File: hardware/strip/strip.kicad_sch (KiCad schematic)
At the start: 39 parts, among them J105 CORTEX-DEBUG, J106 JAE_DX07S016JA3, SW101 SW_Push, SW102 SW_Push, U102 ATSAMD51G, U103 AP2112K-3.3, Y101 32k768

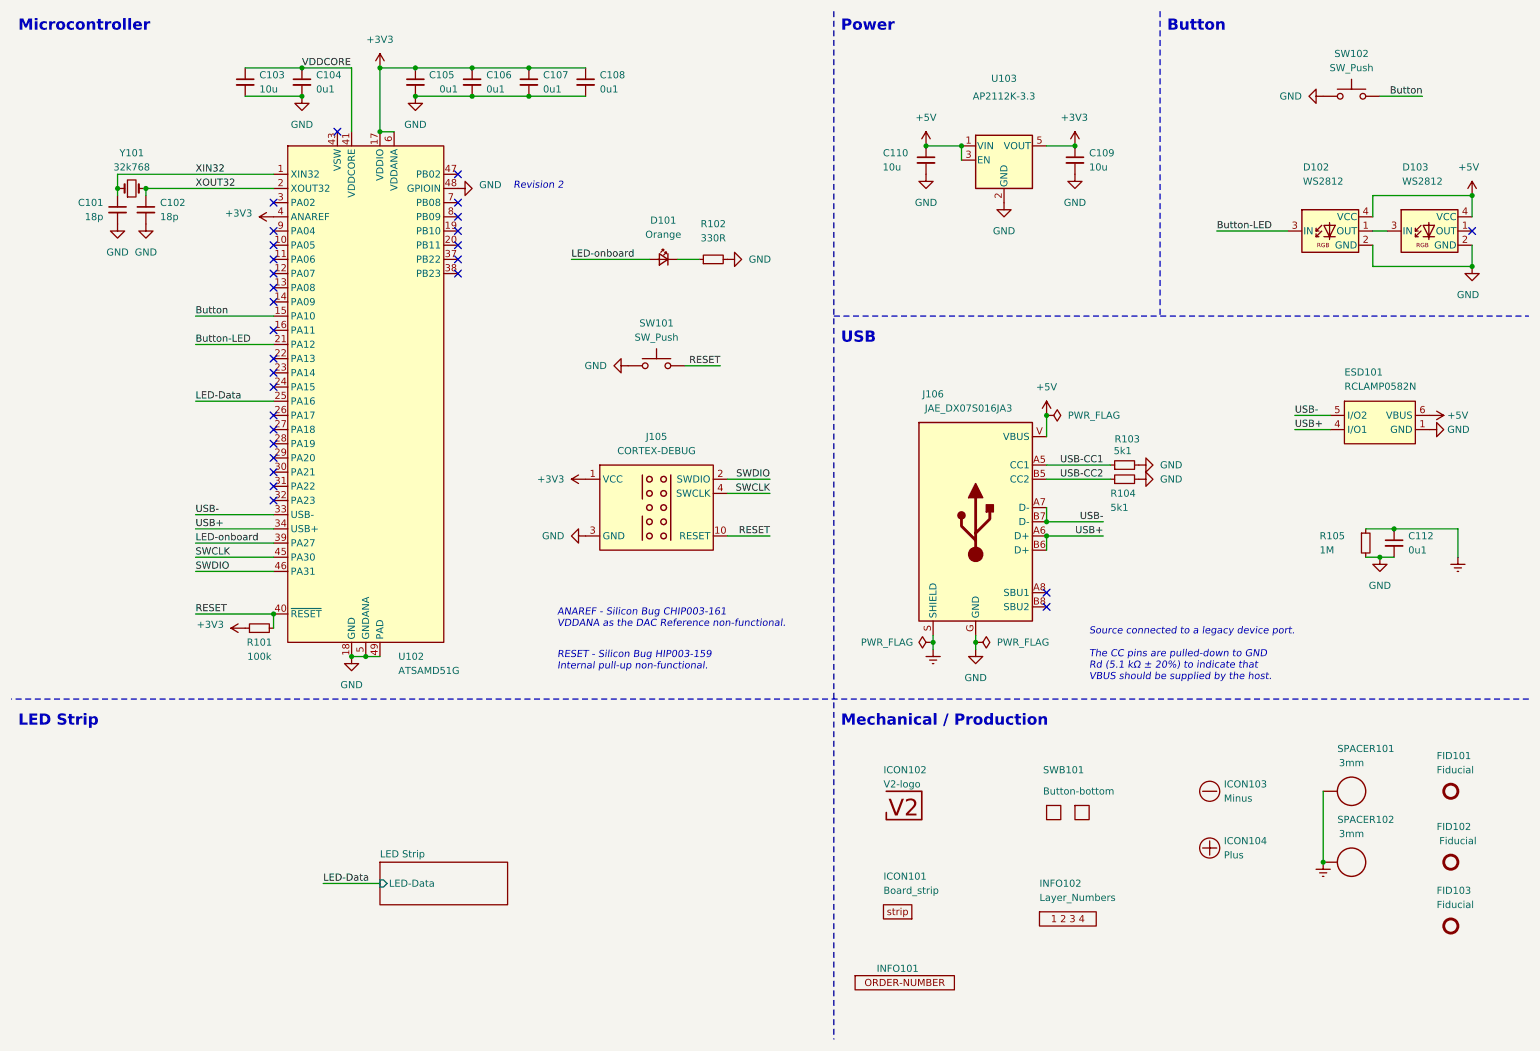
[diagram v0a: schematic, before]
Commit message: Replace Order_Number
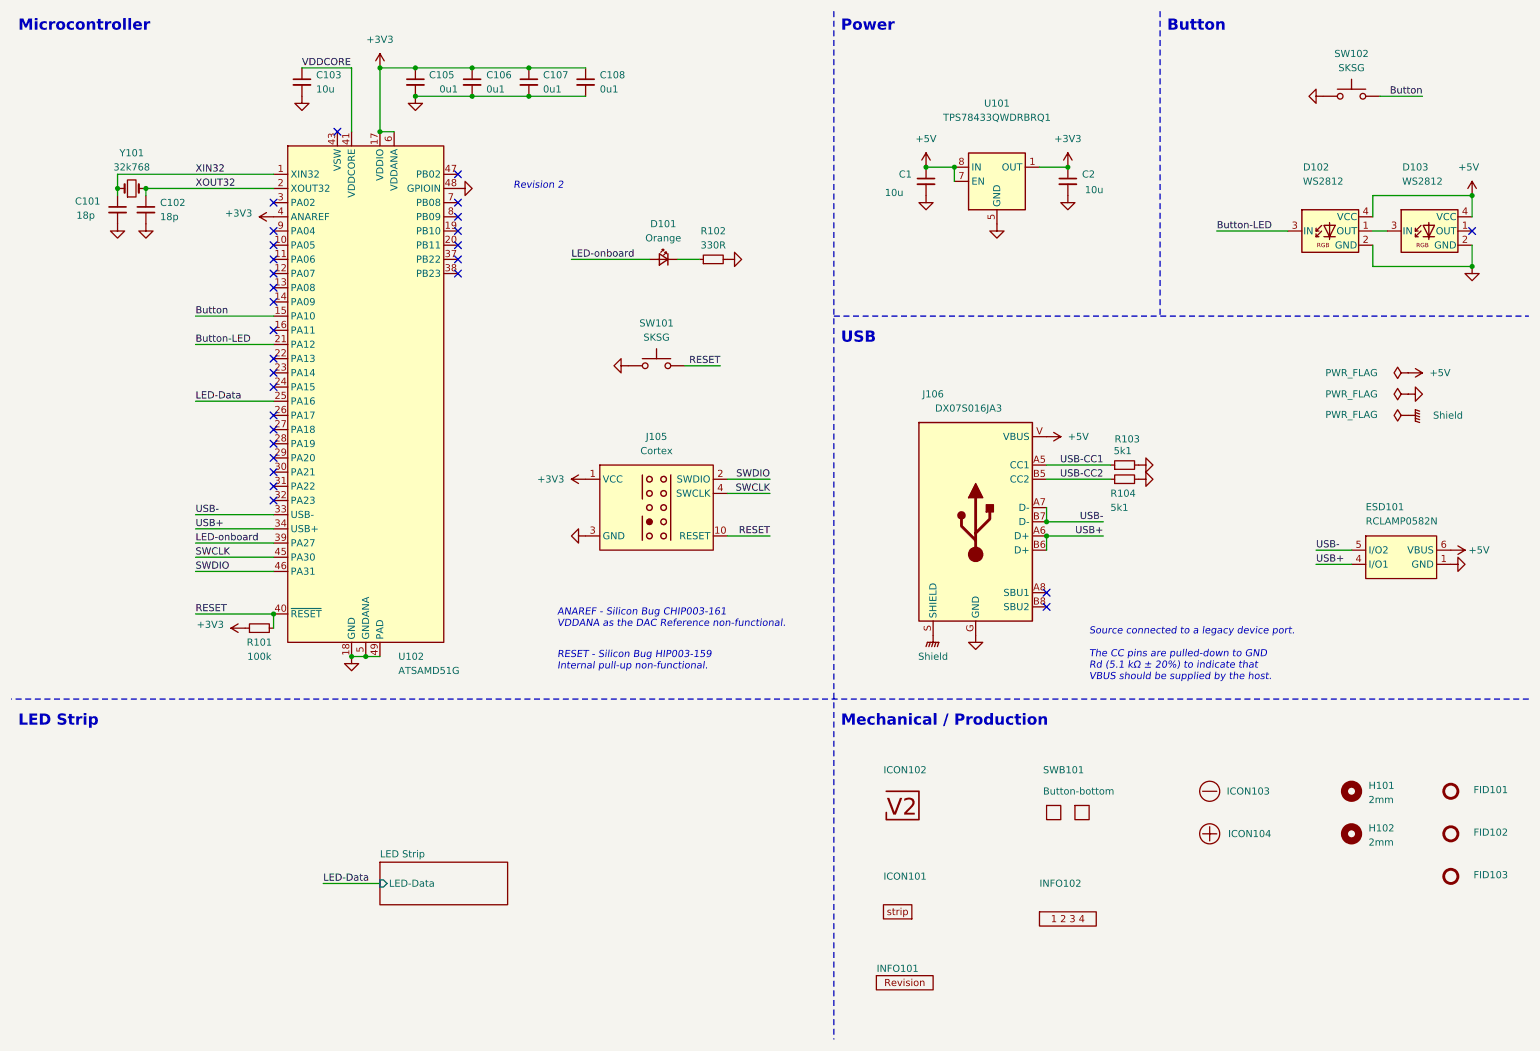
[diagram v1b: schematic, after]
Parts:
- removed C104, C112: 0u1, Capacitor_SMD:C_0603_1608Metric, symbol Device:C_Small
- removed C109, C110: 10u, Capacitor_SMD:C_0603_1608Metric, symbol Device:C_Small
- removed R105: 1M, Resistor_SMD:R_0603_1608Metric, symbol Device:R_Small
- removed SPACER101, SPACER102: 3mm, V2_Spacer_Wurth:9774030243, symbol V2_Spacer_Wurth:9774030243
- removed U103: AP2112K-3.3, Package_TO_SOT_SMD:SOT-23-5, symbol Regulator_Linear:AP2112K-3.3
- added C1, C2: 10u, V2_Capacitor_SMD:C_0805, symbol V2_Device:C_0805_10u
- added H101, H102: 2mm, V2_Mechanical:MountingHole_2mm, symbol V2_Mechanical:MountingHole_2mm
- added U101: TPS78433QWDRBRQ1, V2_Package_SON:VSON-8-1_3x3mm_P0.65_EP1.65x2.4mm, symbol V2_Regulator_Linear:TPS78433QWDRBRQ1
- C101, C102: footprint Capacitor_SMD:C_0603_1608Metric -> V2_Capacitor_SMD:C_0603; symbol Device:C_Small -> V2_Device:C_0603_18p; Manufacturer (none) -> YAGEO; Mouser (none) -> 603-CC603JRNPO9BN180; Product (none) -> CC0603JRNPO9BN180
- C103: footprint Capacitor_SMD:C_0603_1608Metric -> V2_Capacitor_SMD:C_0603; symbol Device:C_Small -> V2_Device:C_0603_10u; Manufacturer (none) -> TDK; Mouser (none) -> 810-C1608X6S1A106M; Product (none) -> C1608X6S1A106M080AC; Rating (none) -> 10V
- C105, C106, C107, C108: footprint Capacitor_SMD:C_0603_1608Metric -> V2_Capacitor_SMD:C_0603; symbol Device:C_Small -> V2_Device:C_0603_0u1; Manufacturer (none) -> TDK; Mouser (none) -> 810-CGA3E2X7R1H104MA; Product (none) -> CGA3E2X7R1H104M080AA; Rating (none) -> 50V
- D101: footprint LED_SMD:LED_0603_1608Metric -> V2_LED:LED_0603; symbol Device:LED_Small -> V2_Device:LED_0603_Orange; Manufacturer (none) -> ROHM Semiconductor; Mouser (none) -> 755-SML-D12D1WT86; Product (none) -> SML-D12D1WT86
- D102, D103: LCSC (none) -> C965555; Manufacturer (none) -> Worldsemi; Product (none) -> WS2812B-2020
- ESD101: Manufacturer (none) -> Semtech; Mouser (none) -> 947-RCLAMP0582N.TCT; Product (none) -> RCLAMP0582N.TCT
- FID101, FID102, FID103: value Fiducial -> Fiducial_Paste
- INFO101: value ORDER-NUMBER -> (none); footprint V2_Production:Order_Number -> V2_Production:Revision; symbol V2_Production:Order_Number -> V2_Production:Revision
- J105: value CORTEX-DEBUG -> Cortex; footprint V2_Cortex_Debug:Cortex_Debug_Pad -> V2_Connector_Debug:Cortex; symbol V2_Cortex_Debug:Cortex_Debug -> V2_Connector_Debug:Cortex
- J106: value JAE_DX07S016JA3 -> DX07S016JA3; Manufacturer (none) -> JAE Electronics; Mouser (none) -> 656-DX07S016JA3R1500; Product (none) -> DX07S016JA3R1500
- R101: footprint Resistor_SMD:R_0603_1608Metric -> V2_Resistor_SMD:R_0603; symbol Device:R_Small -> V2_Device:R_0603_100k; Manufacturer (none) -> Vishay; Mouser (none) -> 71-CRCW0603100KFKEAC; Product (none) -> CRCW0603100KFKEAC; Rating (none) -> 100mW
- R102: footprint Resistor_SMD:R_0603_1608Metric -> V2_Resistor_SMD:R_0603; symbol Device:R_Small -> V2_Device:R_0603_330R; Manufacturer (none) -> Vishay; Mouser (none) -> 71-CRCW0603330RFKEAC; Product (none) -> CRCW0603330RFKEAC; Rating (none) -> 100mW
- R103, R104: footprint Resistor_SMD:R_0603_1608Metric -> V2_Resistor_SMD:R_0603; symbol Device:R_Small -> V2_Device:R_0603_5k1; Manufacturer (none) -> Vishay; Mouser (none) -> 71-CRCW06035K10FKEAC; Product (none) -> CRCW06035K10FKEAC; Rating (none) -> 100mW
- SW101, SW102: value SW_Push -> SKSG; symbol Switch:SW_Push -> V2_Switch:SKSG; Manufacturer (none) -> Alps Alpine; Mouser (none) -> 688-SKSGACE010; Product (none) -> SKSGACE010
- U102: Manufacturer (none) -> Microchip Technology; Mouser (none) -> 556-ATSAMD51G19AMU; Product (none) -> ATSAMD51G19A-MU
- Y101: symbol Device:Crystal_Small -> V2_Device:Crystal_3.2x1.5_32k768; Manufacturer (none) -> ABRACON; Mouser (none) -> 815-ABS0716632.768KT; Product (none) -> ABS07-166-32.768KHZ-T
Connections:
- net +3V3: now also C2.1, U101.1 (OUT)
- net +5V: now also C1.1, U101.7 (EN), U101.8 (IN)
- net GND: now also C1.2, C2.2, U101.5 (GND), U101.9 (GND)
- net Earth renamed Shield
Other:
- moved on the sheet: C103, ESD101, FID102, FID103, ICON104

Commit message: Update Library
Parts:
- C1, C2: symbol V2_Device:C_0805_10u -> V2_Capacitor:0805_10u
- C101, C102: symbol V2_Device:C_0603_18p -> V2_Capacitor:0603_18p
- C103: symbol V2_Device:C_0603_10u -> V2_Capacitor:0603_10u
- C105, C106, C107, C108: symbol V2_Device:C_0603_0u1 -> V2_Capacitor:0603_0u1
- D101: symbol V2_Device:LED_0603_Orange -> V2_LED:0603_Orange
- INFO101: value (none) -> ~
- R101: symbol V2_Device:R_0603_100k -> V2_Resistor:0603_100k
- R102: symbol V2_Device:R_0603_330R -> V2_Resistor:0603_330R
- R103, R104: symbol V2_Device:R_0603_5k1 -> V2_Resistor:0603_5k1
- Y101: symbol V2_Device:Crystal_3.2x1.5_32k768 -> V2_Crystal:3.2x1.5_32k768

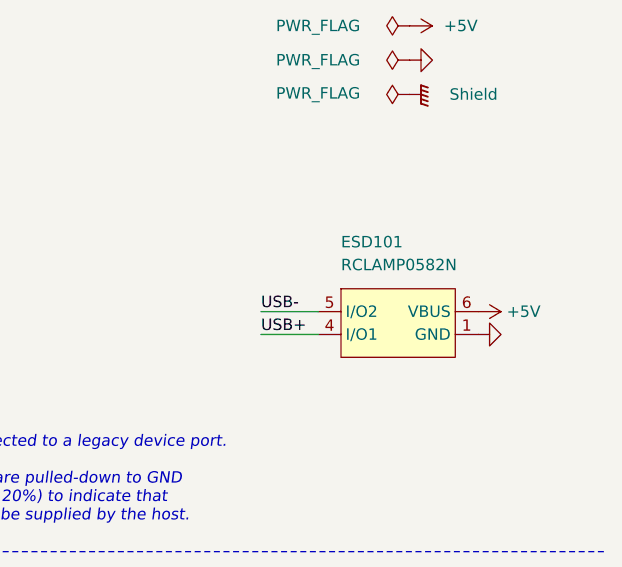
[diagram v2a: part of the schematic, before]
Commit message: Update ESD suppressor
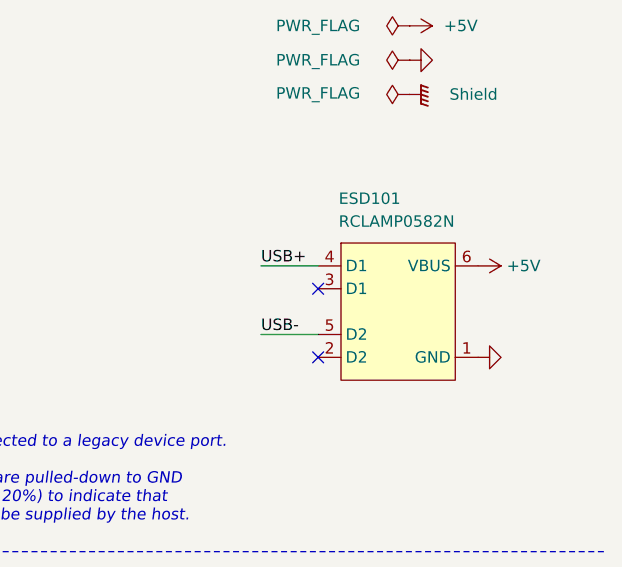
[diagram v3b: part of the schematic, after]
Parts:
- C101, C102: Manufacturer YAGEO -> TDK; Mouser 603-CC603JRNPO9BN180 -> 810-CGA3E2C0G1H180J; Product CC0603JRNPO9BN180 -> CGA3E2C0G1H180J080AA
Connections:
- no-connect marks 29 -> 31
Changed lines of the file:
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@@
 	(title_block
 		(title "V2 strip")
-		(date "2026-02-11")
+		(date "2026-03-14")
 		(rev "2026-02-11")
 		(company "Versio Duo")
@@
 	)
 	(no_connect
+		(at 252.73 106.68)
+	)
+	(no_connect
 		(at 274.32 52.07)
 	)
@@
 		(at 59.69 100.33)
 	)
+	(no_connect
+		(at 252.73 114.3)
+	)
 	(wire
 		(pts
@@
 	(wire
 		(pts
-			(xy 246.38 109.22) (xy 252.73 109.22)
+			(xy 246.38 111.76) (xy 252.73 111.76)
 		)
 		(stroke
@@
 	(wire
 		(pts
-			(xy 73.66 128.27) (xy 76.2 128.27)
+			(xy 246.38 104.14) (xy 252.73 104.14)
 		)
 		(stroke
@@
 	(wire
 		(pts
-			(xy 45.72 110.49) (xy 59.69 110.49)
+			(xy 73.66 128.27) (xy 76.2 128.27)
 		)
 		(stroke
@@
 	(wire
 		(pts
-			(xy 198.12 104.14) (xy 208.28 104.14)
+			(xy 45.72 110.49) (xy 59.69 110.49)
 		)
 		(stroke
@@
 	(wire
 		(pts
-			(xy 78.74 34.29) (xy 81.28 34.29)
+			(xy 198.12 104.14) (xy 208.28 104.14)
 		)
 		(stroke
@@
 	(wire
 		(pts
-			(xy 76.2 128.27) (xy 78.74 128.27)
+			(xy 78.74 34.29) (xy 81.28 34.29)
 		)
 		(stroke
@@
 	(wire
 		(pts
-			(xy 198.12 106.68) (xy 198.12 109.22)
+			(xy 76.2 128.27) (xy 78.74 128.27)
 		)
 		(stroke
@@
 	(wire
 		(pts
-			(xy 45.72 102.87) (xy 59.69 102.87)
+			(xy 198.12 106.68) (xy 198.12 109.22)
 		)
 		(stroke
@@
 	(wire
 		(pts
-			(xy 246.38 111.76) (xy 252.73 111.76)
+			(xy 45.72 102.87) (xy 59.69 102.87)
 		)
 		(stroke
@@
 		)
 	)
+	(label "USB+"
+		(at 246.38 104.14 0)
+		(effects
+			(font
+				(size 1.27 1.27)
+			)
+			(justify left bottom)
+		)
+	)
 	(label "USB-CC2"
 		(at 208.28 96.52 180)
@@
 		)
 	)
-	(label "USB+"
-		(at 246.38 111.76 0)
-		(effects
-			(font
-				(size 1.27 1.27)
-			)
-			(justify left bottom)
-		)
-	)
 	(label "SWDIO"
 		(at 148.59 96.52 180)
@@
 	)
 	(label "USB-"
-		(at 246.38 109.22 0)
+		(at 246.38 111.76 0)
 		(effects
 			(font
@@
 			)
 		)
-		(property "Description" "Resistor, small symbol"
+		(property "Description" ""
 			(at 224.79 93.98 0)
 			(effects
@@
 			)
 		)
-		(property "Description" "Unpolarized capacitor, small symbol"
+		(property "Description" ""
 			(at 115.57 38.1 0)
 			(effects
@@
 		(dnp no)
 		(property "Reference" "ESD101"
-			(at 255.27 102.235 0)
+			(at 255.016 97.409 0)
 			(effects
 				(font
@@
 		)
 		(property "Value" "RCLAMP0582N"
-			(at 255.27 104.775 0)
+			(at 255.016 99.949 0)
 			(effects
 				(font
@@
 		(at 227.33 152.4 0)
 		(unit 1)
-		(exclude_from_sim no)
+		(exclude_from_sim yes)
 		(in_bom no)
 		(on_board yes)
@@
 			)
 		)
-		(property "Sim.Enable" "0"
-			(at 227.33 152.4 0)
-			(effects
-				(font
-					(size 1.27 1.27)
-				)
-				(hide yes)
-			)
-		)
 		(instances
 			(project "strip"
@@
 			)
 		)
-		(property "Description" "Push button switch, generic, two pins"
+		(property "Description" "Push button"
 			(at 252.73 27.94 0)
 			(effects
@@
 	(symbol
 		(lib_id "V2_power:+5V")
-		(at 270.51 109.22 270)
+		(at 270.51 104.14 270)
 		(unit 1)
 		(exclude_from_sim no)
@@
 		(fields_autoplaced yes)
 		(property "Reference" "#PWR130"
-			(at 266.7 109.22 0)
+			(at 266.7 104.14 0)
 			(effects
 				(font
@@
 		)
 		(property "Value" "+5V"
-			(at 273.685 109.2199 90)
+			(at 273.685 104.1399 90)
 			(effects
 				(font
@@
 		)
 		(property "Footprint" ""
-			(at 270.51 109.22 0)
+			(at 270.51 104.14 0)
 			(effects
 				(font
@@
 		)
 		(property "Datasheet" ""
-			(at 270.51 109.22 0)
+			(at 270.51 104.14 0)
 			(effects
 				(font
@@
 		)
 		(property "Description" ""
-			(at 270.51 109.22 0)
+			(at 270.51 104.14 0)
 			(effects
 				(font
@@
 			)
 		)
-		(property "Description" "Light emitting diode, small symbol"
+		(property "Description" ""
 			(at 129.54 62.23 0)
 			(effects
@@
 		(at 201.93 156.21 0)
 		(unit 1)
-		(exclude_from_sim no)
+		(exclude_from_sim yes)
 		(in_bom no)
 		(on_board yes)
@@
 			)
 		)
-		(property "Sim.Enable" "0"
-			(at 201.93 156.21 0)
-			(effects
-				(font
-					(size 1.27 1.27)
-				)
-				(hide yes)
-			)
-		)
 		(instances
 			(project "strip"
@@
 			)
 		)
-		(property "Description" "Unpolarized capacitor, small symbol"
+		(property "Description" ""
 			(at 176.53 56.642 0)
 			(effects
@@
 			)
 		)
-		(property "Description" "Two pin crystal, small symbol"
+		(property "Description" ""
 			(at 34.29 44.45 0)
 			(effects
@@
 			)
 		)
-		(property "Description" "Unpolarized capacitor, small symbol"
+		(property "Description" ""
 			(at 36.83 62.738 0)
 			(effects
@@
 			)
 		)
-		(property "Mouser" "603-CC603JRNPO9BN180"
+		(property "Mouser" "810-CGA3E2C0G1H180J"
 			(at 36.83 71.628 0)
 			(effects
@@
 			)
 		)
-		(property "Product" "CC0603JRNPO9BN180"
+		(property "Product" "CGA3E2C0G1H180J080AA"
 			(at 36.83 68.834 0)
 			(effects
@@
 			)
 		)
-		(property "Manufacturer" "YAGEO"
+		(property "Manufacturer" "TDK"
 			(at 36.83 66.04 0)
 			(effects
@@
 			)
 		)
-		(property "Description" "Unpolarized capacitor, small symbol"
+		(property "Description" ""
 			(at 64.77 40.64 0)
 			(effects
@@
 			)
 		)
-		(property "Description" "Unpolarized capacitor, small symbol"
+		(property "Description" ""
 			(at 31.75 62.738 0)
 			(effects
@@
 			)
 		)
-		(property "Mouser" "603-CC603JRNPO9BN180"
+		(property "Mouser" "810-CGA3E2C0G1H180J"
 			(at 31.75 71.628 0)
 			(effects
@@
 			)
 		)
-		(property "Product" "CC0603JRNPO9BN180"
+		(property "Product" "CGA3E2C0G1H180J080AA"
 			(at 31.75 68.834 0)
 			(effects
@@
 			)
 		)
-		(property "Manufacturer" "YAGEO"
+		(property "Manufacturer" "TDK"
 			(at 31.75 66.04 0)
 			(effects
@@
 			)
 		)
-		(property "Description" "Resistor, small symbol"
+		(property "Description" ""
 			(at 151.13 57.15 0)
 			(effects
@@
 	(symbol
 		(lib_id "V2_power:GND")
-		(at 270.51 111.76 90)
+		(at 270.51 114.3 90)
 		(unit 1)
 		(exclude_from_sim no)
@@
 		(fields_autoplaced yes)
 		(property "Reference" "#PWR131"
-			(at 276.86 111.76 0)
+			(at 276.86 114.3 0)
 			(effects
 				(font
@@
 		)
 		(property "Value" "GND"
-			(at 273.685 111.7599 90)
+			(at 273.685 114.2999 90)
 			(effects
 				(font
@@
 		)
 		(property "Footprint" ""
-			(at 270.51 111.76 0)
+			(at 270.51 114.3 0)
 			(effects
 				(font
@@
 		)
 		(property "Datasheet" ""
-			(at 270.51 111.76 0)
+			(at 270.51 114.3 0)
 			(effects
 				(font
@@
 		)
 		(property "Description" ""
-			(at 270.51 111.76 0)
+			(at 270.51 114.3 0)
 			(effects
 				(font
@@
 			)
 		)
-		(property "Description" "Unpolarized capacitor, small symbol"
+		(property "Description" ""
 			(at 105.41 38.1 0)
 			(effects
@@
 			)
 		)
-		(property "Description" "Unpolarized capacitor, small symbol"
+		(property "Description" ""
 			(at 201.93 56.642 0)
 			(effects
@@
 			)
 		)
-		(property "Description" "Unpolarized capacitor, small symbol"
+		(property "Description" ""
 			(at 85.09 38.1 0)
 			(effects
@@
 			)
 		)
-		(property "Description" "Resistor, small symbol"
+		(property "Description" ""
 			(at 224.79 96.52 0)
 			(effects
@@
 			)
 		)
-		(property "Description" "Push button switch, generic, two pins"
+		(property "Description" "Push button"
 			(at 128.27 76.2 0)
 			(effects
@@
 		(at 171.45 173.99 0)
 		(unit 1)
-		(exclude_from_sim no)
+		(exclude_from_sim yes)
 		(in_bom no)
 		(on_board yes)
@@
 			)
 		)
-		(property "Sim.Enable" "0"
-			(at 171.45 173.99 0)
-			(effects
-				(font
-					(size 1.27 1.27)
-				)
-				(hide yes)
-			)
-		)
 		(instances
 			(project "strip"
@@
 			)
 		)
-		(property "Description" "Unpolarized capacitor, small symbol"
+		(property "Description" ""
 			(at 95.25 38.1 0)
 			(effects
@@
 		(at 227.33 160.02 0)
 		(unit 1)
-		(exclude_from_sim no)
+		(exclude_from_sim yes)
 		(in_bom no)
 		(on_board yes)
@@
 			)
 		)
-		(property "Sim.Enable" "0"
-			(at 227.33 160.02 0)
-			(effects
-				(font
-					(size 1.27 1.27)
-				)
-				(hide yes)
-			)
-		)
 		(instances
 			(project "strip"
@@
 			)
 		)
-		(property "Description" "Resistor, small symbol"
+		(property "Description" ""
 			(at 69.85 123.19 0)
 			(effects

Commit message: Update
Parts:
- C101, C102: Id (none) -> Capacitor:${SYMBOL_NAME}; Rating (none) -> 50V
- C103: Id (none) -> Capacitor:${SYMBOL_NAME}
- C104: renamed from C105; Id (none) -> Capacitor:${SYMBOL_NAME}
- C105: renamed from C106; Id (none) -> Capacitor:${SYMBOL_NAME}
- C106: renamed from C107; Id (none) -> Capacitor:${SYMBOL_NAME}
- C107: renamed from C108; Id (none) -> Capacitor:${SYMBOL_NAME}
- C108: renamed from C1; Id (none) -> Capacitor:${SYMBOL_NAME}
- C109: renamed from C2; Id (none) -> Capacitor:${SYMBOL_NAME}
- D101: Id (none) -> LED:${SYMBOL_NAME}; Rating (none) -> 605nm
- D102, D103: Id (none) -> LED:${SYMBOL_NAME}; Rating (none) -> 15mA
- ESD101: Id (none) -> ESD:${SYMBOL_NAME}; Rating (none) -> 20kV
- INFO101: value ~ -> (none)
- J102: renamed from J106; Id (none) -> USB:${SYMBOL_NAME}; Rating (none) -> USB2.0
- R101, R102, R103, R104: Id (none) -> Resistor:${SYMBOL_NAME}
- SW101, SW102: Id (none) -> Button:${SYMBOL_NAME}; Rating (none) -> 1.6N
- U101: renamed from U102; Id (none) -> MCU:${SYMBOL_NAME}; Rating (none) -> Cortex-M4F
- U102: renamed from U101; Id (none) -> LDO:${SYMBOL_NAME}; Rating (none) -> 300mA
- Y101: Id (none) -> Crystal:${SYMBOL_NAME}; Rating (none) -> 10ppm
- renumbered J105 to J101
